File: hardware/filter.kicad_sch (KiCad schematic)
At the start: 57 parts, among them J2 Pots Main, J3 Pots Front, Q1 KSC1815, Q2 KSC1815, U1 NJM4558D, U2 NJM4558D, U4 NJM4558D, U5 NJM4558D

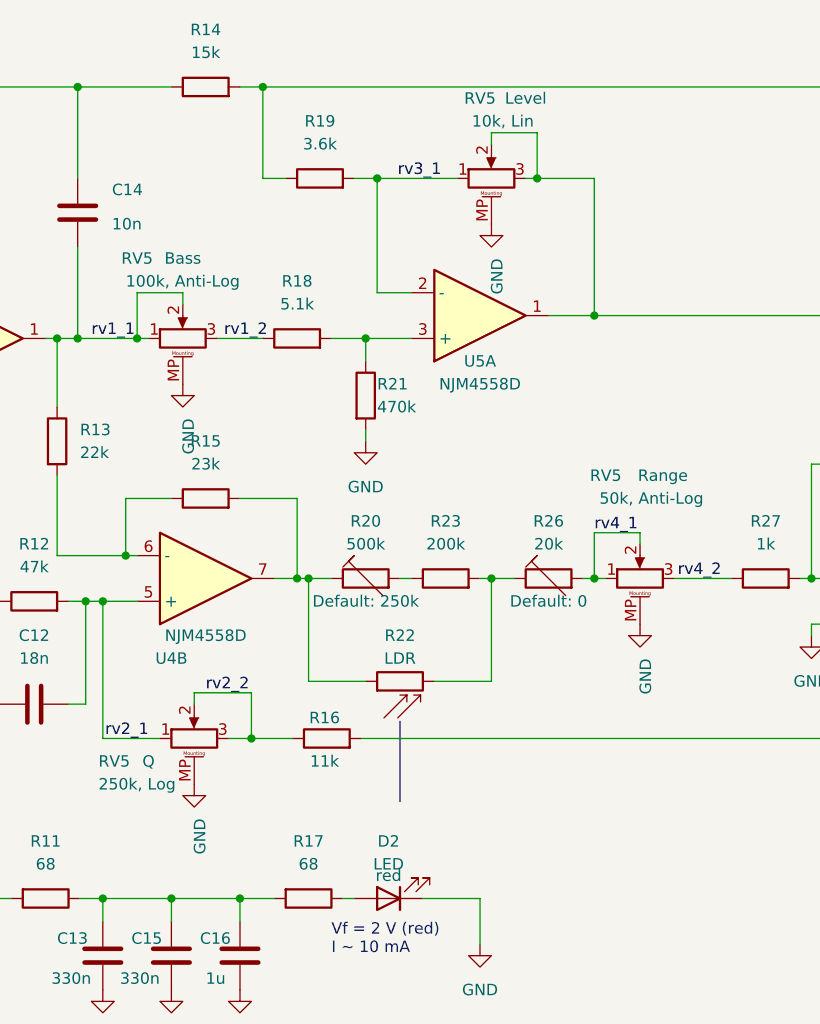
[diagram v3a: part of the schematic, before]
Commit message: Select poti manufacturer and part numbers
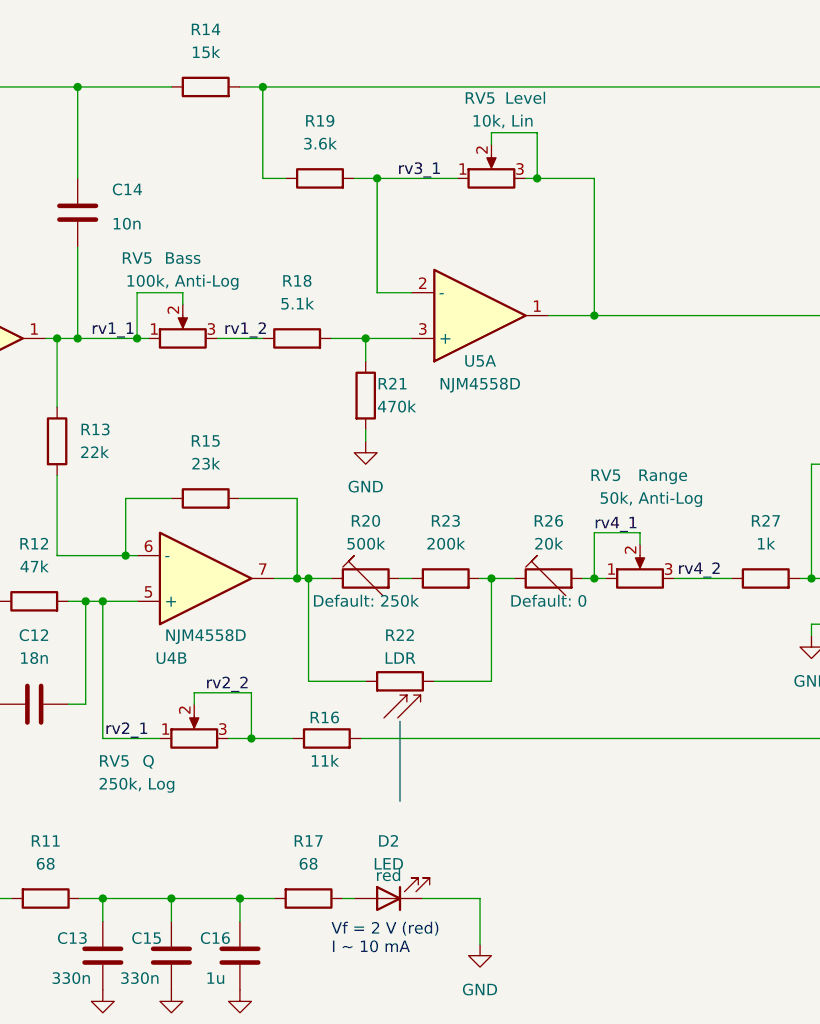
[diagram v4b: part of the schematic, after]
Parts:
- R22: Manufacturer Part Number (none) -> PDV P9004 or PDV 9203; Manufacturers Part Number PDV P9004 or PDV 9203 -> (none)
- RV5: symbol Device:R_Potentiometer_MountingPin -> Device:R_Potentiometer; Manufacturer (none) -> Alpha; Manufacturer Part Number (none) -> RV16AF-20-15K-C100K
- RV5: symbol Device:R_Potentiometer_MountingPin -> Device:R_Potentiometer; Manufacturer (none) -> Alpha; Manufacturer Part Number (none) -> RV16AF-20-15K-B10K
- RV5: symbol Device:R_Potentiometer_MountingPin -> Device:R_Potentiometer; Manufacturer (none) -> Alpha; Manufacturer Part Number (none) -> RV16AF-20-15K-C50K
- RV5: symbol Device:R_Potentiometer_MountingPin -> Device:R_Potentiometer; Manufacturer (none) -> Alpha; Manufacturer Part Number (none) -> RV16AF-20-15K-A250K
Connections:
- net GND: no longer RV5.MP (MountPin), RV5.MP (MountPin), RV5.MP (MountPin), RV5.MP (MountPin)
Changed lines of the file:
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@@
-    )
-  )
-  (symbol (lib_id "power:GND") (at 121.92 115.57 0) (unit 1)
-    (in_bom yes) (on_board yes) (dnp no) (fields_autoplaced)
-    (property "Reference" "#PWR0112" (at 121.92 121.92 0)
-      (effects (font (size 1.27 1.27)) hide)
-    )
-    (property "Value" "GND" (at 122.555 119.38 90)
-      (effects (font (size 1.27 1.27)) (justify right))
-    )
-    (property "Footprint" "" (at 121.92 115.57 0)
-      (effects (font (size 1.27 1.27)) hide)
-    )
-    (property "Datasheet" "" (at 121.92 115.57 0)
-      (effects (font (size 1.27 1.27)) hide)
-    )
-    (pin "1")
-    (instances
-      (project "umidi-wah"
-        (path "/8f66db7e-cf06-4b3a-905e-a75646e85499"
-          (reference "#PWR0112") (unit 1)
-        )
-        (path "/8f66db7e-cf06-4b3a-905e-a75646e85499/159ecef9-3b03-4128-8fe9-708b096478c0"
-          (reference "#PWR026") (unit 1)
-        )
-      )
     )
   )
@@
       (effects (font (size 1.27 1.27)) hide)
     )
-    (property "Manufacturers Part Number" "PDV P9004 or PDV 9203" (at 144.78 104.14 90)
-      (effects (font (size 1.27 1.27)) hide)
-    )
     (property "Supplier" "Digikey" (at 144.78 104.14 90)
+      (effects (font (size 1.27 1.27)) hide)
+    )
+    (property "Manufacturer Part Number" "PDV P9004 or PDV 9203" (at 144.78 104.14 0)
       (effects (font (size 1.27 1.27)) hide)
     )
@@
     )
   )
-  (symbol (lib_id "Device:R_Potentiometer_MountingPin") (at 120.65 66.04 90) (unit 1)
+  (symbol (lib_id "Device:R_Potentiometer") (at 120.65 66.04 90) (unit 1)
     (in_bom yes) (on_board yes) (dnp no)
     (property "Reference" "RV5" (at 115.57 57.15 90)
@@
       (effects (font (size 1.27 1.27)))
     )
+    (property "Manufacturer" "Alpha" (at 120.65 66.04 0)
+      (effects (font (size 1.27 1.27)) hide)
+    )
+    (property "Manufacturer Part Number" "RV16AF-20-15K-C100K" (at 120.65 66.04 0)
+      (effects (font (size 1.27 1.27)) hide)
+    )
     (pin "1")
     (pin "2")
     (pin "3")
-    (pin "MP")
     (instances
       (project "umidi-wah"
@@
     )
   )
-  (symbol (lib_id "Device:R_Potentiometer_MountingPin") (at 154.94 48.26 90) (unit 1)
+  (symbol (lib_id "Device:R_Potentiometer") (at 154.94 48.26 90) (unit 1)
     (in_bom yes) (on_board yes) (dnp no)
     (property "Reference" "RV5" (at 153.67 39.37 90)
@@
       (effects (font (size 1.27 1.27)) hide)
     )
+    (property "Manufacturer" "Alpha" (at 154.94 48.26 0)
+      (effects (font (size 1.27 1.27)) hide)
+    )
+    (property "Manufacturer Part Number" "RV16AF-20-15K-B10K" (at 154.94 48.26 0)
+      (effects (font (size 1.27 1.27)) hide)
+    )
     (pin "1")
     (pin "2")
     (pin "3")
-    (pin "MP")
     (instances
       (project "umidi-wah"
@@
     )
   )
-  (symbol (lib_id "power:GND") (at 171.45 97.79 0) (unit 1)
-    (in_bom yes) (on_board yes) (dnp no) (fields_autoplaced)
-    (property "Reference" "#PWR0112" (at 171.45 104.14 0)
-      (effects (font (size 1.27 1.27)) hide)
-    )
-    (property "Value" "GND" (at 172.085 101.6 90)
-      (effects (font (size 1.27 1.27)) (justify right))
-    )
-    (property "Footprint" "" (at 171.45 97.79 0)
-      (effects (font (size 1.27 1.27)) hide)
-    )
-    (property "Datasheet" "" (at 171.45 97.79 0)
-      (effects (font (size 1.27 1.27)) hide)
-    )
-    (pin "1")
-    (instances
-      (project "umidi-wah"
-        (path "/8f66db7e-cf06-4b3a-905e-a75646e85499"
-          (reference "#PWR0112") (unit 1)
-        )
-        (path "/8f66db7e-cf06-4b3a-905e-a75646e85499/159ecef9-3b03-4128-8fe9-708b096478c0"
-          (reference "#PWR025") (unit 1)
-        )
-      )
-    )
-  )
   (symbol (lib_id "power:GND") (at 239.395 140.97 0) (unit 1)
     (in_bom yes) (on_board yes) (dnp no) (fields_autoplaced)
@@
     )
   )
-  (symbol (lib_id "power:GND") (at 154.94 53.34 0) (unit 1)
-    (in_bom yes) (on_board yes) (dnp no) (fields_autoplaced)
-    (property "Reference" "#PWR0112" (at 154.94 59.69 0)
-      (effects (font (size 1.27 1.27)) hide)
-    )
-    (property "Value" "GND" (at 155.575 57.15 90)
-      (effects (font (size 1.27 1.27)) (justify right))
-    )
-    (property "Footprint" "" (at 154.94 53.34 0)
-      (effects (font (size 1.27 1.27)) hide)
-    )
-    (property "Datasheet" "" (at 154.94 53.34 0)
-      (effects (font (size 1.27 1.27)) hide)
-    )
-    (pin "1")
-    (instances
-      (project "umidi-wah"
-        (path "/8f66db7e-cf06-4b3a-905e-a75646e85499"
-          (reference "#PWR0112") (unit 1)
-        )
-        (path "/8f66db7e-cf06-4b3a-905e-a75646e85499/159ecef9-3b03-4128-8fe9-708b096478c0"
-          (reference "#PWR024") (unit 1)
-        )
-      )
-    )
-  )
-  (symbol (lib_id "Device:R_Potentiometer_MountingPin") (at 171.45 92.71 90) (unit 1)
+  (symbol (lib_id "Device:R_Potentiometer") (at 171.45 92.71 90) (unit 1)
     (in_bom yes) (on_board yes) (dnp no)
     (property "Reference" "RV5" (at 167.64 81.28 90)
@@
       (effects (font (size 1.27 1.27)) hide)
     )
+    (property "Manufacturer" "Alpha" (at 171.45 92.71 0)
+      (effects (font (size 1.27 1.27)) hide)
+    )
+    (property "Manufacturer Part Number" "RV16AF-20-15K-C50K" (at 171.45 92.71 0)
+      (effects (font (size 1.27 1.27)) hide)
+    )
     (pin "1")
     (pin "2")
     (pin "3")
-    (pin "MP")
     (instances
       (project "umidi-wah"
@@
     )
   )
-  (symbol (lib_id "Device:R_Potentiometer_MountingPin") (at 121.92 110.49 90) (unit 1)
+  (symbol (lib_id "Device:R_Potentiometer") (at 121.92 110.49 90) (unit 1)
     (in_bom yes) (on_board yes) (dnp no)
     (property "Reference" "RV5" (at 113.03 113.03 90)
@@
       (effects (font (size 1.27 1.27)))
     )
+    (property "Manufacturer" "Alpha" (at 121.92 110.49 0)
+      (effects (font (size 1.27 1.27)) hide)
+    )
+    (property "Manufacturer Part Number" "RV16AF-20-15K-A250K" (at 121.92 110.49 0)
+      (effects (font (size 1.27 1.27)) hide)
+    )
     (pin "1")
     (pin "2")
     (pin "3")
-    (pin "MP")
     (instances
       (project "umidi-wah"
@@
         )
       )
-    )
-  )
-  (symbol (lib_id "power:GND") (at 120.65 71.12 0) (unit 1)
-    (in_bom yes) (on_board yes) (dnp no) (fields_autoplaced)
-    (property "Reference" "#PWR0112" (at 120.65 77.47 0)
-      (effects (font (size 1.27 1.27)) hide)
-    )
-    (property "Value" "GND" (at 121.285 74.93 90)
-      (effects (font (size 1.27 1.27)) (justify right))
-    )
-    (property "Footprint" "" (at 120.65 71.12 0)
-      (effects (font (size 1.27 1.27)) hide)
-    )
-    (property "Datasheet" "" (at 120.65 71.12 0)
-      (effects (font (size 1.27 1.27)) hide)
-    )
-    (pin "1")
-    (instances
-      (project "umidi-wah"
-        (path "/8f66db7e-cf06-4b3a-905e-a75646e85499"
-          (reference "#PWR0112") (unit 1)
-        )
-        (path "/8f66db7e-cf06-4b3a-905e-a75646e85499/159ecef9-3b03-4128-8fe9-708b096478c0"
-          (reference "#PWR023") (unit 1)
-        )
-      )
